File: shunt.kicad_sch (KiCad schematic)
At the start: 10 parts, among them U11 LMP8645HV, U12 LMP8645HV

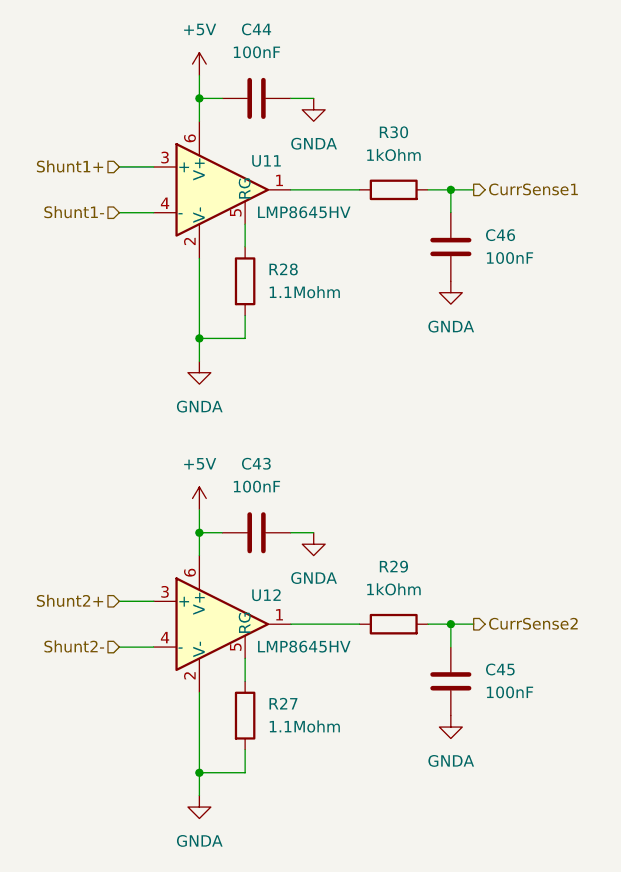
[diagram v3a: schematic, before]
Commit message: assigned footprints, some minor schematic stuff, started layout
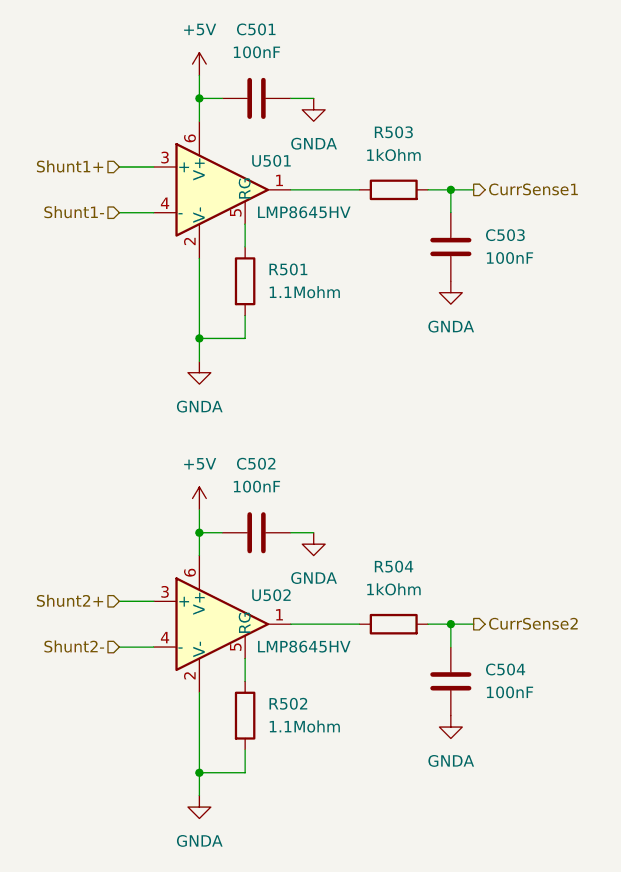
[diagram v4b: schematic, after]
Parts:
- C501: renamed from C44; footprint (none) -> Capacitor_SMD:C_0603_1608Metric
- C502: renamed from C43; footprint (none) -> Capacitor_SMD:C_0603_1608Metric
- C503: renamed from C46; footprint (none) -> Capacitor_SMD:C_0603_1608Metric
- C504: renamed from C45; footprint (none) -> Capacitor_SMD:C_0603_1608Metric
- R501: renamed from R28; footprint (none) -> Resistor_SMD:R_0603_1608Metric
- R502: renamed from R27; footprint (none) -> Resistor_SMD:R_0603_1608Metric
- R503: renamed from R30; footprint (none) -> Resistor_SMD:R_0603_1608Metric
- R504: renamed from R29; footprint (none) -> Resistor_SMD:R_0603_1608Metric
- renumbered U11 to U501, U12 to U502
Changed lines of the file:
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@@
 		(dnp no)
 		(fields_autoplaced yes)
-		(property "Reference" "#PWR062"
+		(property "Reference" "#PWR0501"
 			(at 128.27 68.58 0)
 			(hide yes)
@@
 			(project "LV_DCDC"
 				(path "/ccad4640-78c7-423b-83df-3ec0b90aa2b3/31d4a71c-66fd-4b80-a697-70e62f2ea215"
-					(reference "#PWR062")
+					(reference "#PWR0501")
 					(unit 1)
 				)
@@
 		(dnp no)
 		(fields_autoplaced yes)
-		(property "Reference" "R27"
+		(property "Reference" "R502"
 			(at 135.89 134.6199 0)
 			(show_name no)
@@
 			)
 		)
-		(property "Footprint" ""
+		(property "Footprint" "Resistor_SMD:R_0603_1608Metric"
 			(at 131.572 135.89 90)
 			(hide yes)
@@
 			(project "LV_DCDC"
 				(path "/ccad4640-78c7-423b-83df-3ec0b90aa2b3/31d4a71c-66fd-4b80-a697-70e62f2ea215"
-					(reference "R27")
+					(reference "R502")
 					(unit 1)
 				)
@@
 		(dnp no)
 		(fields_autoplaced yes)
-		(property "Reference" "#PWR064"
+		(property "Reference" "#PWR0504"
 			(at 128.27 151.13 0)
 			(hide yes)
@@
 			(project "LV_DCDC"
 				(path "/ccad4640-78c7-423b-83df-3ec0b90aa2b3/31d4a71c-66fd-4b80-a697-70e62f2ea215"
-					(reference "#PWR064")
+					(reference "#PWR0504")
 					(unit 1)
 				)
@@
 		(dnp no)
 		(fields_autoplaced yes)
-		(property "Reference" "R30"
+		(property "Reference" "R503"
 			(at 149.86 71.12 90)
 			(show_name no)
@@
 			)
 		)
-		(property "Footprint" ""
+		(property "Footprint" "Resistor_SMD:R_0603_1608Metric"
 			(at 149.86 79.248 90)
 			(hide yes)
@@
 			(project "LV_DCDC"
 				(path "/ccad4640-78c7-423b-83df-3ec0b90aa2b3/31d4a71c-66fd-4b80-a697-70e62f2ea215"
-					(reference "R30")
+					(reference "R503")
 					(unit 1)
 				)
@@
 		(dnp no)
 		(fields_autoplaced yes)
-		(property "Reference" "R29"
+		(property "Reference" "R504"
 			(at 149.86 119.38 90)
 			(show_name no)
@@
 			)
 		)
-		(property "Footprint" ""
+		(property "Footprint" "Resistor_SMD:R_0603_1608Metric"
 			(at 149.86 127.508 90)
 			(hide yes)
@@
 			(project "LV_DCDC"
 				(path "/ccad4640-78c7-423b-83df-3ec0b90aa2b3/31d4a71c-66fd-4b80-a697-70e62f2ea215"
-					(reference "R29")
+					(reference "R504")
 					(unit 1)
 				)
@@
 		(dnp no)
 		(fields_autoplaced yes)
-		(property "Reference" "#PWR063"
+		(property "Reference" "#PWR0503"
 			(at 128.27 116.84 0)
 			(hide yes)
@@
 			(project "LV_DCDC"
 				(path "/ccad4640-78c7-423b-83df-3ec0b90aa2b3/31d4a71c-66fd-4b80-a697-70e62f2ea215"
-					(reference "#PWR063")
+					(reference "#PWR0503")
 					(unit 1)
 				)
@@
 		(dnp no)
 		(fields_autoplaced yes)
-		(property "Reference" "#PWR068"
+		(property "Reference" "#PWR0508"
 			(at 156.21 142.24 0)
 			(hide yes)
@@
 			(project "LV_DCDC"
 				(path "/ccad4640-78c7-423b-83df-3ec0b90aa2b3/31d4a71c-66fd-4b80-a697-70e62f2ea215"
-					(reference "#PWR068")
+					(reference "#PWR0508")
 					(unit 1)
 				)
@@
 		(in_pos_files yes)
 		(dnp no)
-		(property "Reference" "U11"
+		(property "Reference" "U501"
 			(at 133.985 74.295 0)
 			(show_name no)
@@
 			(project "LV_DCDC"
 				(path "/ccad4640-78c7-423b-83df-3ec0b90aa2b3/31d4a71c-66fd-4b80-a697-70e62f2ea215"
-					(reference "U11")
+					(reference "U501")
 					(unit 1)
 				)
@@
 		(dnp no)
 		(fields_autoplaced yes)
-		(property "Reference" "C44"
+		(property "Reference" "C501"
 			(at 134.62 59.69 90)
 			(show_name no)
@@
 			)
 		)
-		(property "Footprint" ""
+		(property "Footprint" "Capacitor_SMD:C_0603_1608Metric"
 			(at 138.43 66.3448 0)
 			(hide yes)
@@
 			(project "LV_DCDC"
 				(path "/ccad4640-78c7-423b-83df-3ec0b90aa2b3/31d4a71c-66fd-4b80-a697-70e62f2ea215"
-					(reference "C44")
+					(reference "C501")
 					(unit 1)
 				)
@@
 		(dnp no)
 		(fields_autoplaced yes)
-		(property "Reference" "R28"
+		(property "Reference" "R501"
 			(at 135.89 86.3599 0)
 			(show_name no)
@@
 			)
 		)
-		(property "Footprint" ""
+		(property "Footprint" "Resistor_SMD:R_0603_1608Metric"
 			(at 131.572 87.63 90)
 			(hide yes)
@@
 			(project "LV_DCDC"
 				(path "/ccad4640-78c7-423b-83df-3ec0b90aa2b3/31d4a71c-66fd-4b80-a697-70e62f2ea215"
-					(reference "R28")
+					(reference "R501")
 					(unit 1)
 				)
@@
 		(dnp no)
 		(fields_autoplaced yes)
-		(property "Reference" "#PWR069"
+		(property "Reference" "#PWR0507"
 			(at 156.21 93.98 0)
 			(hide yes)
@@
 			(project "LV_DCDC"
 				(path "/ccad4640-78c7-423b-83df-3ec0b90aa2b3/31d4a71c-66fd-4b80-a697-70e62f2ea215"
-					(reference "#PWR069")
+					(reference "#PWR0507")
 					(unit 1)
 				)
@@
 		(dnp no)
 		(fields_autoplaced yes)
-		(property "Reference" "#PWR066"
+		(property "Reference" "#PWR0506"
 			(at 140.97 121.92 0)
 			(hide yes)
@@
 			(project "LV_DCDC"
 				(path "/ccad4640-78c7-423b-83df-3ec0b90aa2b3/31d4a71c-66fd-4b80-a697-70e62f2ea215"
-					(reference "#PWR066")
+					(reference "#PWR0506")
 					(unit 1)
 				)
@@
 		(in_pos_files yes)
 		(dnp no)
-		(property "Reference" "U12"
+		(property "Reference" "U502"
 			(at 133.985 122.555 0)
 			(show_name no)
@@
 			(project "LV_DCDC"
 				(path "/ccad4640-78c7-423b-83df-3ec0b90aa2b3/31d4a71c-66fd-4b80-a697-70e62f2ea215"
-					(reference "U12")
+					(reference "U502")
 					(unit 1)
 				)
@@
 		(dnp no)
 		(fields_autoplaced yes)
-		(property "Reference" "C46"
+		(property "Reference" "C503"
 			(at 160.02 82.5499 0)
 			(show_name no)
@@
 			)
 		)
-		(property "Footprint" ""
+		(property "Footprint" "Capacitor_SMD:C_0603_1608Metric"
 			(at 157.1752 87.63 0)
 			(hide yes)
@@
 			(project "LV_DCDC"
 				(path "/ccad4640-78c7-423b-83df-3ec0b90aa2b3/31d4a71c-66fd-4b80-a697-70e62f2ea215"
-					(reference "C46")
+					(reference "C503")
 					(unit 1)
 				)
@@
 		(dnp no)
 		(fields_autoplaced yes)
-		(property "Reference" "C43"
+		(property "Reference" "C502"
 			(at 134.62 107.95 90)
 			(show_name no)
@@
 			)
 		)
-		(property "Footprint" ""
+		(property "Footprint" "Capacitor_SMD:C_0603_1608Metric"
 			(at 138.43 114.6048 0)
 			(hide yes)
@@
 			(project "LV_DCDC"
 				(path "/ccad4640-78c7-423b-83df-3ec0b90aa2b3/31d4a71c-66fd-4b80-a697-70e62f2ea215"
-					(reference "C43")
+					(reference "C502")
 					(unit 1)
 				)
@@
 		(dnp no)
 		(fields_autoplaced yes)
-		(property "Reference" "#PWR065"
+		(property "Reference" "#PWR0502"
 			(at 128.27 102.87 0)
 			(hide yes)
@@
 			(project "LV_DCDC"
 				(path "/ccad4640-78c7-423b-83df-3ec0b90aa2b3/31d4a71c-66fd-4b80-a697-70e62f2ea215"
-					(reference "#PWR065")
+					(reference "#PWR0502")
 					(unit 1)
 				)
@@
 		(dnp no)
 		(fields_autoplaced yes)
-		(property "Reference" "C45"
+		(property "Reference" "C504"
 			(at 160.02 130.8099 0)
 			(show_name no)
@@
 			)
 		)
-		(property "Footprint" ""
+		(property "Footprint" "Capacitor_SMD:C_0603_1608Metric"
 			(at 157.1752 135.89 0)
 			(hide yes)
@@
 			(project "LV_DCDC"
 				(path "/ccad4640-78c7-423b-83df-3ec0b90aa2b3/31d4a71c-66fd-4b80-a697-70e62f2ea215"
-					(reference "C45")
+					(reference "C504")
 					(unit 1)
 				)
@@
 		(dnp no)
 		(fields_autoplaced yes)
-		(property "Reference" "#PWR067"
+		(property "Reference" "#PWR0505"
 			(at 140.97 73.66 0)
 			(hide yes)
@@
 			(project "LV_DCDC"
 				(path "/ccad4640-78c7-423b-83df-3ec0b90aa2b3/31d4a71c-66fd-4b80-a697-70e62f2ea215"
-					(reference "#PWR067")
-					(unit 1)
-				)
+					(reference "#PWR0505")
+					(unit 1)
+				)
